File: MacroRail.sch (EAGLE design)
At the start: 18 parts, among them CN1 1X4-3.5MM, J1 SJ1-2503A, U1 ESP32DEVKITC, U2 TCM2209-V1.2

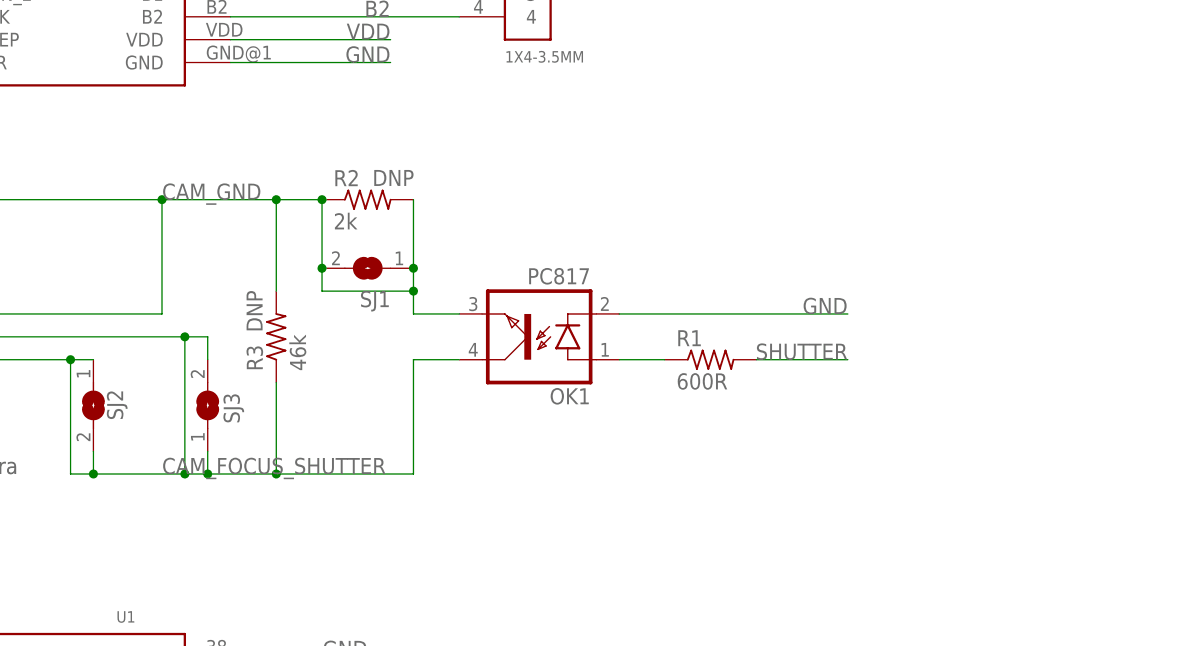
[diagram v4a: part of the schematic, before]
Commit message: Documentation update
Initial attempt to describe the camera shutter circuitry.
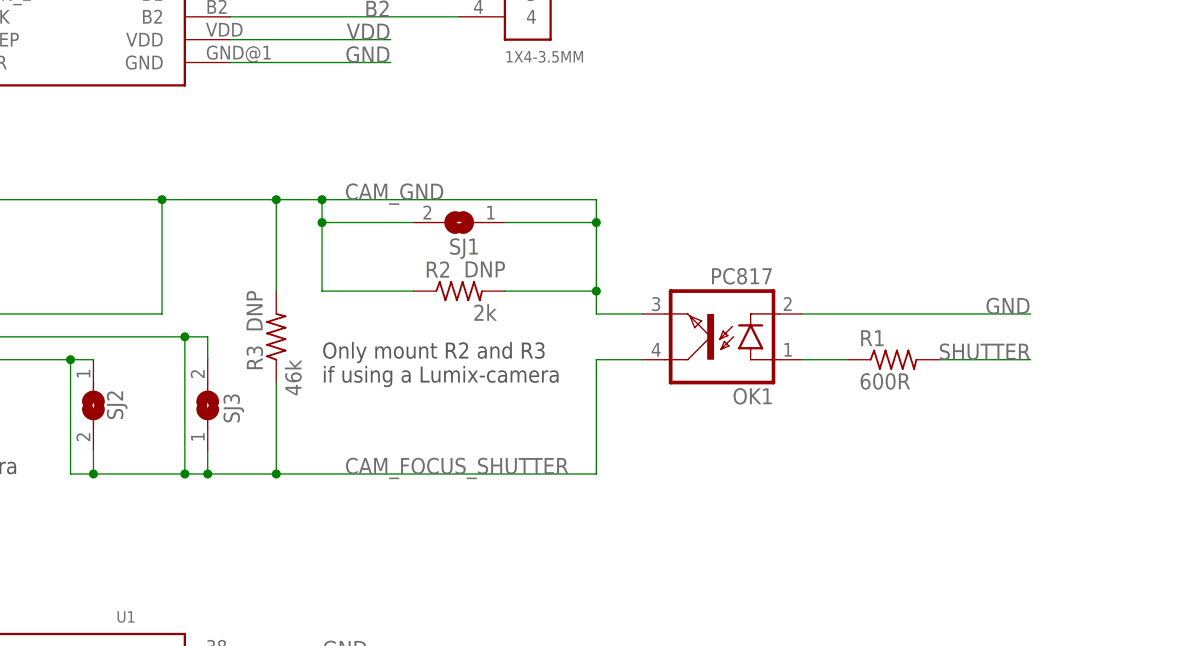
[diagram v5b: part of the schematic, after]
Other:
- note added: "Only mount R2 and R3 if using a Lumix-camera"
- moved on the sheet: OK1, R1, R2, SJ1
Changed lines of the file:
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@@
 <wire x1="-21.082" y1="87.376" x2="-20.32" y2="90.678" width="0.1524" layer="97"/>
 <wire x1="-20.32" y1="83.82" x2="-20.32" y2="87.376" width="0.1524" layer="97"/>
+<text x="30.48" y="88.9" size="1.778" layer="97">Only mount R2 and R3
+if using a Lumix-camera</text>
 </plain>
 <instances>
@@
 <attribute name="VALUE" x="29.591" y="150.876" size="1.778" layer="96" rot="R90"/>
 </instance>
-<instance part="R1" gate="G$1" x="73.66" y="91.44" smashed="yes">
-<attribute name="NAME" x="69.85" y="92.9386" size="1.778" layer="95"/>
-<attribute name="VALUE" x="69.85" y="88.138" size="1.778" layer="96"/>
+<instance part="R1" gate="G$1" x="93.98" y="91.44" smashed="yes">
+<attribute name="NAME" x="90.17" y="92.9386" size="1.778" layer="95"/>
+<attribute name="VALUE" x="90.17" y="88.138" size="1.778" layer="96"/>
 </instance>
 <instance part="CN1" gate="G$1" x="50.8" y="134.62" smashed="yes">
@@
 <attribute name="VALUE" x="171.45" y="68.58" size="1.778" layer="96" rot="R180"/>
 </instance>
-<instance part="OK1" gate="A" x="53.34" y="93.98" smashed="yes" rot="R180">
-<attribute name="NAME" x="60.325" y="88.265" size="1.778" layer="95" rot="R180"/>
-<attribute name="VALUE" x="60.325" y="101.6" size="1.778" layer="96" rot="R180"/>
+<instance part="OK1" gate="A" x="73.66" y="93.98" smashed="yes" rot="R180">
+<attribute name="NAME" x="80.645" y="88.265" size="1.778" layer="95" rot="R180"/>
+<attribute name="VALUE" x="80.645" y="101.6" size="1.778" layer="96" rot="R180"/>
 </instance>
 <instance part="R3" gate="G$1" x="25.4" y="93.98" smashed="yes" rot="R90">
 <attribute name="NAME" x="23.9014" y="90.17" size="1.778" layer="95" rot="R90"/>
-<attribute name="VALUE" x="28.702" y="90.17" size="1.778" layer="96" rot="R90"/>
+<attribute name="VALUE" x="28.194" y="87.376" size="1.778" layer="96" rot="R90"/>
 <attribute name="DNP" x="23.876" y="94.488" size="1.778" layer="96" rot="R90" display="name"/>
 </instance>
-<instance part="R2" gate="G$1" x="35.56" y="109.22" smashed="yes">
-<attribute name="NAME" x="31.75" y="110.7186" size="1.778" layer="95"/>
-<attribute name="VALUE" x="31.75" y="105.918" size="1.778" layer="96"/>
-<attribute name="DNP" x="36.068" y="110.744" size="1.778" layer="96" display="name"/>
+<instance part="R2" gate="G$1" x="45.72" y="99.06" smashed="yes">
+<attribute name="NAME" x="41.91" y="100.5586" size="1.778" layer="95"/>
+<attribute name="VALUE" x="47.244" y="95.758" size="1.778" layer="96"/>
+<attribute name="DNP" x="46.228" y="100.584" size="1.778" layer="96" display="name"/>
 </instance>
 <instance part="SJ2" gate="1" x="5.08" y="86.36" smashed="yes" rot="R270">
@@
 <attribute name="VALUE" x="21.59" y="83.82" size="1.778" layer="96" rot="R90"/>
 </instance>
-<instance part="SJ1" gate="1" x="35.56" y="101.6" smashed="yes" rot="R180">
-<attribute name="NAME" x="38.1" y="99.06" size="1.778" layer="95" rot="R180"/>
-<attribute name="VALUE" x="38.1" y="105.41" size="1.778" layer="96" rot="R180"/>
+<instance part="SJ1" gate="1" x="45.72" y="106.68" smashed="yes" rot="R180">
+<attribute name="NAME" x="48.006" y="104.902" size="1.778" layer="95" rot="R180"/>
+<attribute name="VALUE" x="48.26" y="110.49" size="1.778" layer="96" rot="R180"/>
 </instance>
 <instance part="J1" gate="G$1" x="-35.56" y="99.06" smashed="yes">
@@
 <net name="CAM_GND" class="0">
 <segment>
-<wire x1="30.48" y1="109.22" x2="25.4" y2="109.22" width="0.1524" layer="91"/>
 <wire x1="25.4" y1="109.22" x2="12.7" y2="109.22" width="0.1524" layer="91"/>
 <pinref part="JP1" gate="A" pin="3"/>
 <wire x1="12.7" y1="109.22" x2="12.7" y2="96.52" width="0.1524" layer="91"/>
 <wire x1="12.7" y1="96.52" x2="-12.7" y2="96.52" width="0.1524" layer="91"/>
-<label x="12.7" y="109.22" size="1.778" layer="95"/>
+<label x="33.02" y="109.22" size="1.778" layer="95"/>
 <pinref part="R2" gate="G$1" pin="1"/>
 <pinref part="R3" gate="G$1" pin="2"/>
@@
 <junction x="25.4" y="109.22"/>
 <pinref part="SJ1" gate="1" pin="2"/>
-<wire x1="30.48" y1="101.6" x2="30.48" y2="109.22" width="0.1524" layer="91"/>
-<junction x="30.48" y="109.22"/>
 <pinref part="OK1" gate="A" pin="EMIT"/>
 <pinref part="R2" gate="G$1" pin="2"/>
-<wire x1="40.64" y1="109.22" x2="40.64" y2="101.6" width="0.1524" layer="91"/>
-<wire x1="40.64" y1="101.6" x2="40.64" y2="99.06" width="0.1524" layer="91"/>
-<wire x1="40.64" y1="99.06" x2="40.64" y2="96.52" width="0.1524" layer="91"/>
-<wire x1="40.64" y1="96.52" x2="45.72" y2="96.52" width="0.1524" layer="91"/>
+<wire x1="60.96" y1="109.22" x2="60.96" y2="106.68" width="0.1524" layer="91"/>
+<wire x1="60.96" y1="106.68" x2="60.96" y2="99.06" width="0.1524" layer="91"/>
+<wire x1="60.96" y1="99.06" x2="60.96" y2="96.52" width="0.1524" layer="91"/>
+<wire x1="60.96" y1="96.52" x2="66.04" y2="96.52" width="0.1524" layer="91"/>
 <pinref part="SJ1" gate="1" pin="1"/>
-<junction x="40.64" y="101.6"/>
-<wire x1="30.48" y1="101.6" x2="30.48" y2="99.06" width="0.1524" layer="91"/>
-<junction x="30.48" y="101.6"/>
-<wire x1="30.48" y1="99.06" x2="40.64" y2="99.06" width="0.1524" layer="91"/>
-<junction x="40.64" y="99.06"/>
+<junction x="60.96" y="106.68"/>
+<wire x1="30.48" y1="109.22" x2="60.96" y2="109.22" width="0.1524" layer="91"/>
 <pinref part="J1" gate="G$1" pin="1"/>
 <wire x1="-35.56" y1="99.06" x2="-27.94" y2="99.06" width="0.1524" layer="91"/>
@@
 <wire x1="-27.94" y1="109.22" x2="12.7" y2="109.22" width="0.1524" layer="91"/>
 <junction x="12.7" y="109.22"/>
+<wire x1="25.4" y1="109.22" x2="30.48" y2="109.22" width="0.1524" layer="91"/>
+<junction x="30.48" y="109.22"/>
+<wire x1="50.8" y1="99.06" x2="60.96" y2="99.06" width="0.1524" layer="91"/>
+<junction x="60.96" y="99.06"/>
+<wire x1="50.8" y1="106.68" x2="60.96" y2="106.68" width="0.1524" layer="91"/>
+<wire x1="30.48" y1="109.22" x2="30.48" y2="106.68" width="0.1524" layer="91"/>
+<wire x1="30.48" y1="106.68" x2="30.48" y2="99.06" width="0.1524" layer="91"/>
+<wire x1="30.48" y1="99.06" x2="40.64" y2="99.06" width="0.1524" layer="91"/>
+<wire x1="40.64" y1="106.68" x2="30.48" y2="106.68" width="0.1524" layer="91"/>
+<junction x="30.48" y="106.68"/>
 </segment>
 </net>
@@
 <pinref part="JP1" gate="A" pin="1"/>
 <wire x1="2.54" y1="91.44" x2="-12.7" y2="91.44" width="0.1524" layer="91"/>
-<label x="12.7" y="78.74" size="1.778" layer="95"/>
+<label x="33.02" y="78.74" size="1.778" layer="95"/>
 <pinref part="SJ2" gate="1" pin="2"/>
 <pinref part="SJ2" gate="1" pin="1"/>
@@
 <wire x1="15.24" y1="93.98" x2="15.24" y2="78.74" width="0.1524" layer="91"/>
 <pinref part="OK1" gate="A" pin="COL"/>
-<wire x1="40.64" y1="91.44" x2="45.72" y2="91.44" width="0.1524" layer="91"/>
-<wire x1="40.64" y1="78.74" x2="40.64" y2="91.44" width="0.1524" layer="91"/>
-<wire x1="25.4" y1="78.74" x2="40.64" y2="78.74" width="0.1524" layer="91"/>
+<wire x1="60.96" y1="91.44" x2="66.04" y2="91.44" width="0.1524" layer="91"/>
+<wire x1="60.96" y1="78.74" x2="60.96" y2="91.44" width="0.1524" layer="91"/>
+<wire x1="25.4" y1="78.74" x2="60.96" y2="78.74" width="0.1524" layer="91"/>
 <pinref part="R3" gate="G$1" pin="1"/>
 <wire x1="25.4" y1="88.9" x2="25.4" y2="78.74" width="0.1524" layer="91"/>
@@
 <segment>
 <pinref part="OK1" gate="A" pin="C"/>
-<wire x1="63.5" y1="96.52" x2="88.9" y2="96.52" width="0.1524" layer="91"/>
-<label x="88.9" y="96.52" size="1.778" layer="95" rot="MR0"/>
+<wire x1="83.82" y1="96.52" x2="109.22" y2="96.52" width="0.1524" layer="91"/>
+<label x="109.22" y="96.52" size="1.778" layer="95" rot="MR0"/>
 </segment>
 <segment>
@@
 <segment>
 <pinref part="R1" gate="G$1" pin="2"/>
-<wire x1="78.74" y1="91.44" x2="88.9" y2="91.44" width="0.1524" layer="91"/>
-<label x="88.9" y="91.44" size="1.778" layer="95" rot="MR0"/>
+<wire x1="99.06" y1="91.44" x2="109.22" y2="91.44" width="0.1524" layer="91"/>
+<label x="109.22" y="91.44" size="1.778" layer="95" rot="MR0"/>
 </segment>
 </net>
@@
 <pinref part="OK1" gate="A" pin="A"/>
 <pinref part="R1" gate="G$1" pin="1"/>
-<wire x1="63.5" y1="91.44" x2="68.58" y2="91.44" width="0.1524" layer="91"/>
-</segment>
-</net>
+<wire x1="83.82" y1="91.44" x2="88.9" y2="91.44" width="0.1524" layer="91"/>
+</segment>
+</net>

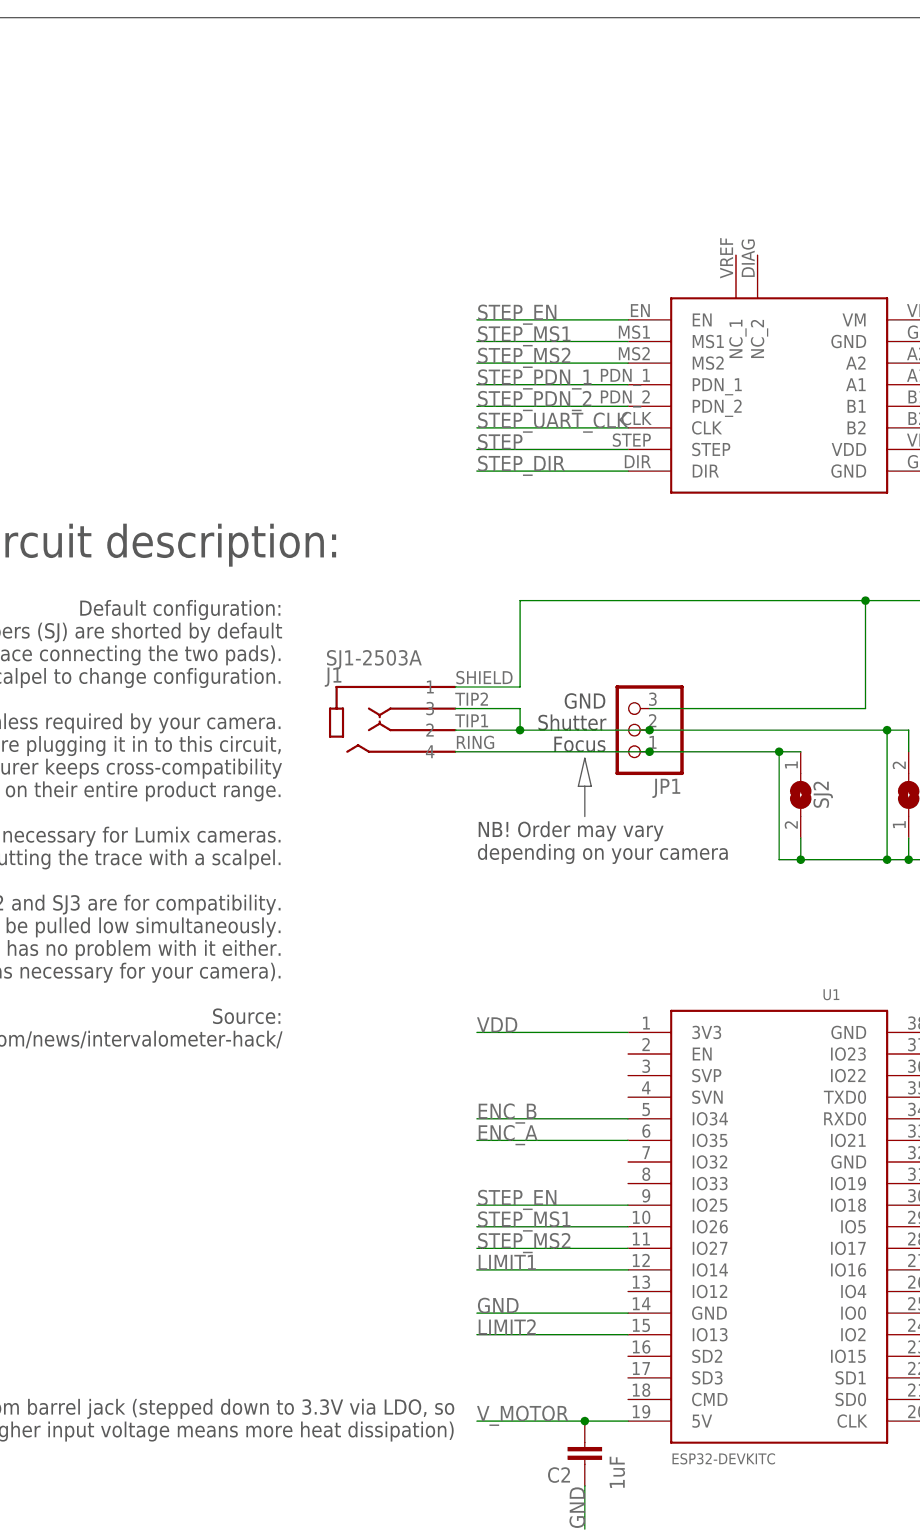
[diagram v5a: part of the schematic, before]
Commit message: Start V1.1 design
Add UART Communication between TCM and ESP via SD2 and SD3 pins. Connect DIAG pin. Still undecided whether INDEX pin is necessary as this pin is not always easily accessible on TCM boards.
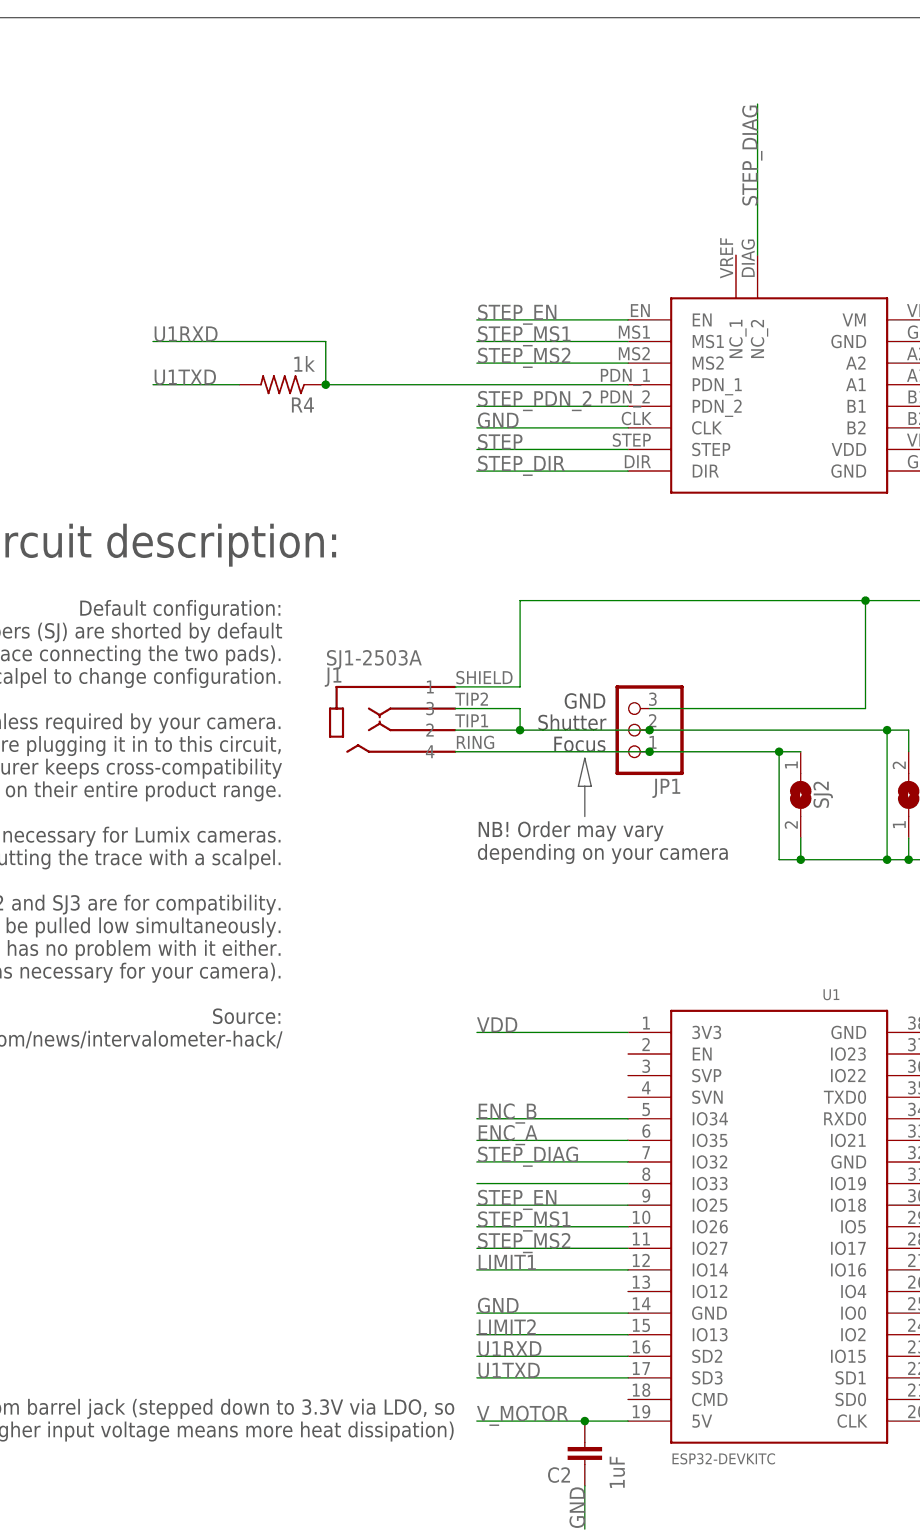
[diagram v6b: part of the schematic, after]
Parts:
- added R4: 1k, rcl:R-US_0207/7
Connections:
- removed net STEP_PDN_1: U2.PDN_1
- removed net STEP_UART_CLK: U2.CLK
- new net N$2: U1.IO33
- new net STEP_DIAG: U1.IO32, U2.NC_2
- new net U1RXD: R4.1, U1.SD2, U2.PDN_1
- new net U1TXD: R4.2, U1.SD3
- net GND: now also U2.CLK
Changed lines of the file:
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@@
 <part name="J1" library="00-Random-Components-Simen" library_urn="urn:adsk.eagle:library:24319138" deviceset="SJ1-2503A" device="" package3d_urn="urn:adsk.eagle:package:34317647/3" override_package3d_urn="urn:adsk.eagle:package:34319661/2" override_package_urn="urn:adsk.eagle:footprint:34317645/1" override_locally_modified="yes"/>
 <part name="C2" library="rcl" library_urn="urn:adsk.eagle:library:334" deviceset="C-EU" device="050-024X044" package3d_urn="urn:adsk.eagle:package:23643/1" override_package3d_urn="urn:adsk.eagle:package:34322317/2" override_package_urn="urn:adsk.eagle:footprint:23147/1" value="1uF"/>
+<part name="R4" library="rcl" library_urn="urn:adsk.eagle:library:334" deviceset="R-US_" device="0207/7" package3d_urn="urn:adsk.eagle:package:23493/2" value="1k"/>
 </parts>
 <sheets>
@@
 <attribute name="VALUE" x="-17.399" y="8.636" size="1.778" layer="96" rot="R270"/>
 </instance>
+<instance part="R4" gate="G$1" x="-55.88" y="134.62" smashed="yes" rot="R180">
+<attribute name="NAME" x="-52.07" y="133.1214" size="1.778" layer="95" rot="R180"/>
+<attribute name="VALUE" x="-52.07" y="137.922" size="1.778" layer="96" rot="R180"/>
+</instance>
 </instances>
 <busses>
@@
 <label x="-20.32" y="0" size="1.778" layer="95" rot="R90"/>
 </segment>
+<segment>
+<pinref part="U2" gate="G$1" pin="CLK"/>
+<wire x1="-15.24" y1="129.54" x2="-33.02" y2="129.54" width="0.1524" layer="91"/>
+<label x="-33.02" y="129.54" size="1.778" layer="95"/>
+</segment>
 </net>
 <net name="A2" class="1">
@@
 </segment>
 </net>
-<net name="STEP_PDN_1" class="0">
-<segment>
-<pinref part="U2" gate="G$1" pin="PDN_1"/>
-<wire x1="-15.24" y1="134.62" x2="-33.02" y2="134.62" width="0.1524" layer="91"/>
-<label x="-33.02" y="134.62" size="1.778" layer="95"/>
-</segment>
-</net>
 <net name="STEP_PDN_2" class="0">
 <segment>
@@
 </segment>
 </net>
-<net name="STEP_UART_CLK" class="0">
-<segment>
-<pinref part="U2" gate="G$1" pin="CLK"/>
-<wire x1="-15.24" y1="129.54" x2="-33.02" y2="129.54" width="0.1524" layer="91"/>
-<label x="-33.02" y="129.54" size="1.778" layer="95"/>
-</segment>
-</net>
 <net name="STEP" class="0">
 <segment>
@@
 <pinref part="R1" gate="G$1" pin="1"/>
 <wire x1="83.82" y1="91.44" x2="88.9" y2="91.44" width="0.1524" layer="91"/>
+</segment>
+</net>
+<net name="U1TXD" class="0">
+<segment>
+<pinref part="R4" gate="G$1" pin="2"/>
+<wire x1="-60.96" y1="134.62" x2="-71.12" y2="134.62" width="0.1524" layer="91"/>
+<label x="-71.12" y="134.62" size="1.778" layer="95"/>
+</segment>
+<segment>
+<pinref part="U1" gate="G$1" pin="SD3"/>
+<wire x1="-33.02" y1="17.78" x2="-15.24" y2="17.78" width="0.1524" layer="91"/>
+<label x="-33.02" y="17.78" size="1.778" layer="95"/>
+</segment>
+</net>
+<net name="U1RXD" class="0">
+<segment>
+<pinref part="R4" gate="G$1" pin="1"/>
+<wire x1="-50.8" y1="134.62" x2="-50.8" y2="139.7" width="0.1524" layer="91"/>
+<wire x1="-50.8" y1="139.7" x2="-71.12" y2="139.7" width="0.1524" layer="91"/>
+<junction x="-50.8" y="134.62"/>
+<label x="-71.12" y="139.7" size="1.778" layer="95"/>
+<wire x1="-50.8" y1="134.62" x2="-15.24" y2="134.62" width="0.1524" layer="91"/>
+<pinref part="U2" gate="G$1" pin="PDN_1"/>
+</segment>
+<segment>
+<pinref part="U1" gate="G$1" pin="SD2"/>
+<wire x1="-15.24" y1="20.32" x2="-33.02" y2="20.32" width="0.1524" layer="91"/>
+<label x="-33.02" y="20.32" size="1.778" layer="95"/>
+</segment>
+</net>
+<net name="STEP_DIAG" class="0">
+<segment>
+<pinref part="U2" gate="G$1" pin="NC_2"/>
+<wire x1="0" y1="149.86" x2="0" y2="167.64" width="0.1524" layer="91"/>
+<label x="0" y="167.64" size="1.778" layer="95" rot="R90" align="bottom-right"/>
+</segment>
+<segment>
+<pinref part="U1" gate="G$1" pin="IO32"/>
+<wire x1="-15.24" y1="43.18" x2="-33.02" y2="43.18" width="0.1524" layer="91"/>
+<label x="-33.02" y="43.18" size="1.778" layer="95"/>
+</segment>
+</net>
+<net name="N$2" class="0">
+<segment>
+<pinref part="U1" gate="G$1" pin="IO33"/>
+<wire x1="-15.24" y1="40.64" x2="-33.02" y2="40.64" width="0.1524" layer="91"/>
 </segment>
 </net>
@@
 for full support of SPICE simulation.
 </note>
+<note version="9.0" severity="warning">
+Since Version 9.0, EAGLE supports the align property for labels.
+Labels in schematic will not be understood with this version. Update EAGLE to the latest version
+for full support of labels.
+</note>
 </compatibility>
